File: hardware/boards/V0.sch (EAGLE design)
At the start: 61 parts, among them IC2 TPS6300, J1 SJ-43515TS-SMT, J2 HIROSE_DM3BT-DSF-PEJSHIROSE_D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, J3 MOLEX_105450-0101MOLEX_105450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, Q1 MC-306, Q2 ON_SEMI_MMBT5551LT1GON_SEMI_M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, U1 VS1053-L, X1 PG203J, X3 FH12-45S-0.5SH

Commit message: checkpoint: USB
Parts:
- added C21: 0.1uF, rcl:C-USC0805K
- added C22, C24: 4.7uF, rcl:CPOL-USC/6032-28R
- added C23, C25: 0.1uF, rcl:CPOL-USC/6032-28R
- added CENTER_SW, DOWN_SW, LEFT_SW, RIGHT_SW, UP_SW: E-SWITCH_TL3315NF160QE-SWITCH_TL3315NF160Q_0_0, E-Switch-TL3315NF160Q:E-SWITCH_TL3315NF160QE-SWITCH_TL3315NF160Q_0_0
- added D10, D8, D9: ON_SEMICONDUCTOR_ESD5Z5.0T1GON_SEMICONDUCTOR_ESD5Z5.0T1G_0_0, ESD-Diode_On-Semi-ESD5Z5.0T1G:ON_SEMICONDUCTOR_ESD5Z5.0T1GON_SEMICONDUCTOR_ESD5Z5.0T1G_0_0
- added D3, D4, D5, D6, D7: (no value), adafruit:DIODESOD-523
- added R19, R25, R33: 5k, rcl:R-US_R0805
- added R20: 15k, rcl:R-US_R0805
- added R21: 35k, rcl:R-US_R0805
- added R22: 75k, rcl:R-US_R0805
- added R23: 155k, rcl:R-US_R0805
- added R24: 50k, rcl:R-US_R0805
- added R26, R32: 10k, rcl:R-US_R0805
- added R27, R28: 5.1k, rcl:R-US_R0805
- added R29: 22.1k, rcl:R-US_R0805
- added R30: 47.5k, rcl:R-US_R0805
- added R31: 1k, rcl:R-US_R0805
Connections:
- new net BUTTON_ADC: R19.1, R20.1, R21.1, R22.1, R23.1, R25.2
- new net BUTTON_DIN: C21.2, R24.2
- new net CP_VDD: C24.+, C25.+, JL.VDD, R31.2
- new net N$16: D3.A, LEFT_SW.4, R19.2
- new net N$24: D4.A, R20.2, UP_SW.4
- new net N$28: D5.A, R21.2, RIGHT_SW.4
- new net N$29: D6.A, DOWN_SW.4, R22.2
- new net N$32: D3.C, D4.C, D5.C, D6.C, D7.C, R24.1, R26.2
- new net N$49: CENTER_SW.4, D7.A, R23.2
- new net N$50: J3.CC1, R27.1
- new net N$51: J3.CC2, R28.1
- new net N$52: JL.VBUS, R29.1, R30.2
- new net N$53: JL.RSTB, R31.1
- new net USB_D+: D9.K, J3.1_D+, J3.2_D+, JL.D+
- new net USB_D-: D8.K, J3.1_D-, J3.2_D-, JL.D-
- new net VBAT_ADC_IN: R32.2, R33.1
- new net VBUS: D10.K, J3.1_VBUS, J3.2_VBUS, J3.3_VBUS, J3.4_VBUS, R29.2
- net GND: now also C22.-, C23.-, C24.-, C25.-, D10.A, D8.A, D9.A, J3.1_GND, J3.2_GND, J3.3_GND, J3.4_GND, J3.MNT_1, J3.MNT_2, J3.MNT_3, J3.MNT_4, R25.1, R26.1, R27.2, R28.2, R30.1, R32.1
- net V3P3: now also C21.1, CENTER_SW.2, D1.COMMON_ANODE, DOWN_SW.2, LEFT_SW.2, RIGHT_SW.2, UP_SW.2
- net VBAT: now also C22.+, C23.+, JL.VREGIN, R33.2
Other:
- note added: "CC1"
- note added: "CC2"

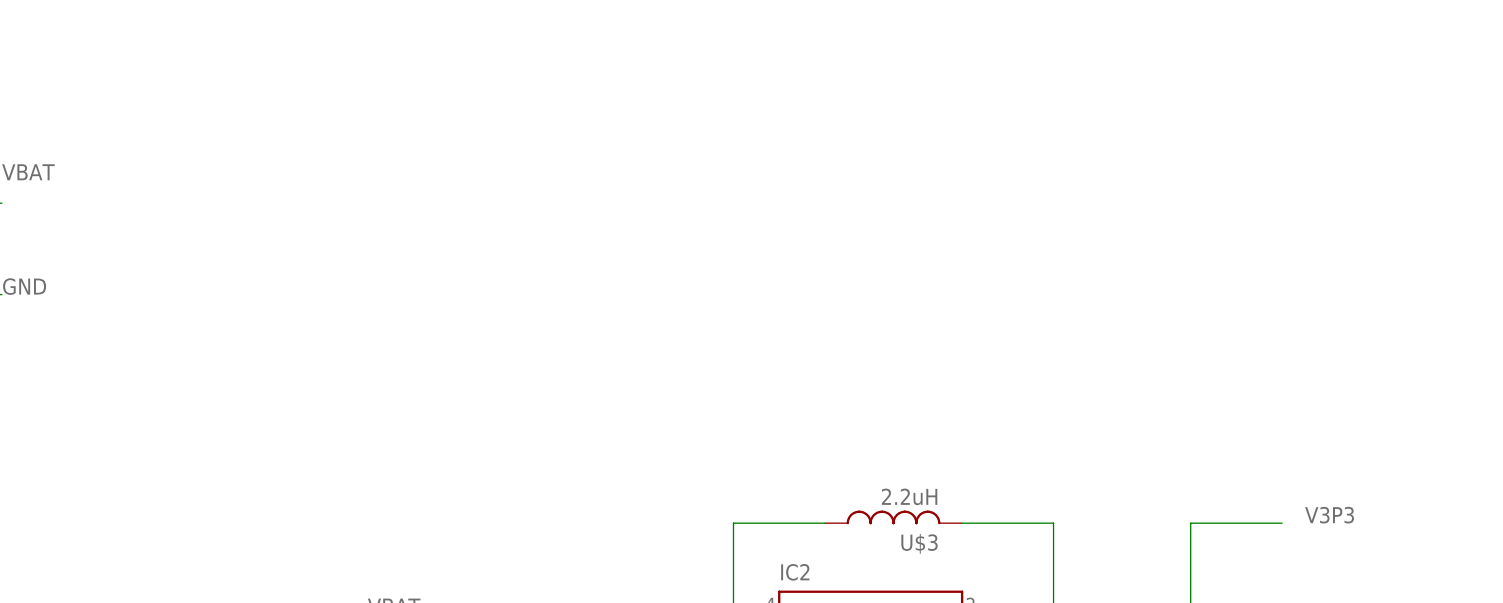
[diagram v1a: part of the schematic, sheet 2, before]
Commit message: checkpoint: LED, battery voltage circuit, charge IC, half of the CP2102N
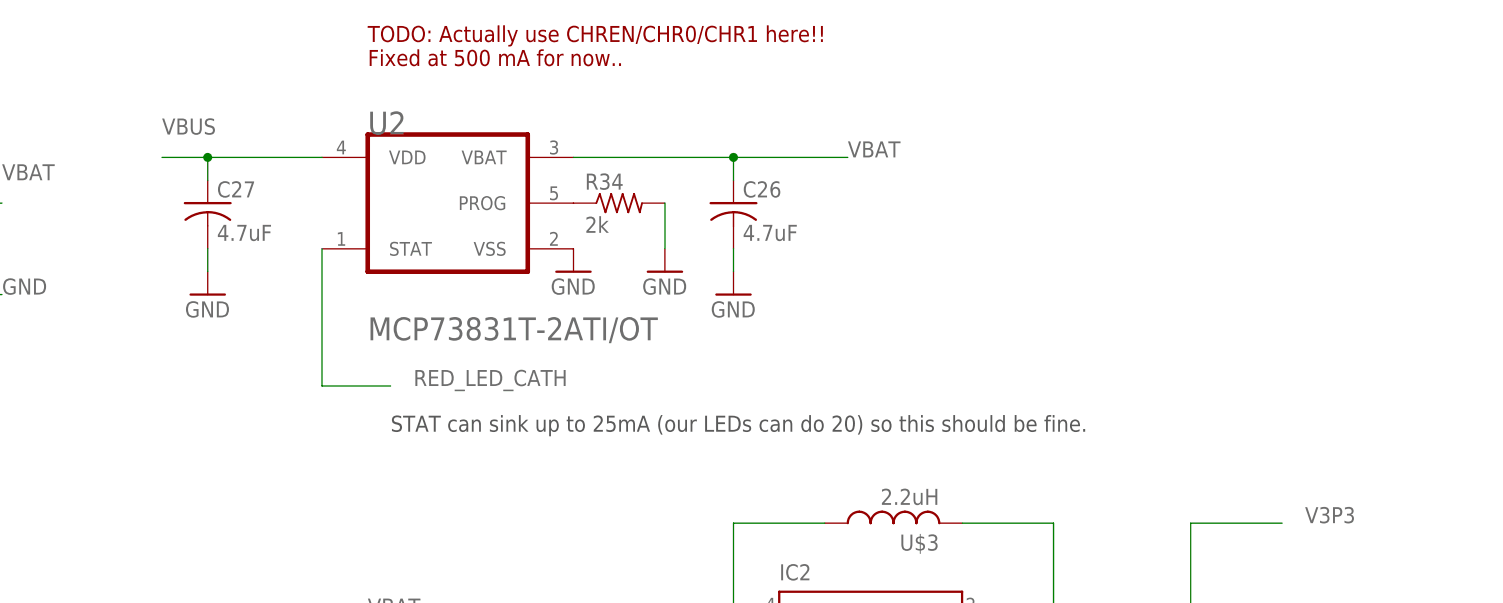
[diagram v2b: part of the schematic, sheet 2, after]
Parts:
- added C26, C27: 4.7uF, rcl:C-USC0805
- added R34: 2k, rcl:R-US_R0805
- added R35: 100, rcl:R-US_R0805
- added R36: (no value), rcl:R-US_R0805
- added U2: MICROCHIP_MCP73831T-2ATI-OTMICROCHIP_MCP73831T-2ATI-OT_0_1, Microchip-MCP73831T-2ATI:MICROCHIP_MCP73831T-2ATI-OTMICROCHIP_MCP73831T-2ATI-OT_0_1
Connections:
- new net BLUE_LED_CATH: D1.BLUE_CATHODE
- new net GREEN_LED_CATH: R36.2
- new net N$54: R34.1, U2.PROG
- new net N$55: D1.RED_CATHODE, R35.1
- new net N$56: D1.GREEN_CATHODE, R36.1
- new net RED_LED_CATH: R35.2, U2.STAT
- net GND: now also C26.2, C27.2, R34.2, U2.VSS
- net VBAT: now also C26.1, U2.VBAT
- net VBUS: now also C27.1, U2.VDD
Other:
- note added: "Blue has a voltage drop of ~3.7V which is greater than our regulated voltage so we won't bother with a current limiting resistor."
- note added: "Green LED (AlInGaP Green on the C113) has a drop of about 2.3 volts also on about 20mA. 1.0 volts for 20mA = V / I = R = 1 / 20mA = 50 ohms"
- note added: "Red LED has a 1.9V drop and 20mA, so: 1.4V for 20mA = V / I = R = 1.4V / 20mA = 70 ohms since we don't want to blind people let's call it an even 100"
- note added: "STAT can sink up to 25mA (our LEDs can do 20) so this should be fine."
- note added: "TODO: Actually use CHREN/CHR0/CHR1 here!! Fixed at 500 mA for now.."
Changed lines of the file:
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@@
 <part name="R32" library="rcl" library_urn="urn:adsk.eagle:library:334" deviceset="R-US_" device="R0805" package3d_urn="urn:adsk.eagle:package:23553/2" value="10k"/>
 <part name="R33" library="rcl" library_urn="urn:adsk.eagle:library:334" deviceset="R-US_" device="R0805" package3d_urn="urn:adsk.eagle:package:23553/2" value="5k"/>
+<part name="U2" library="Microchip-MCP73831T-2ATI" deviceset="MICROCHIP_MCP73831T-2ATI-OT" device="MICROCHIP_MCP73831T-2ATI-OT_0_1"/>
+<part name="C26" library="rcl" library_urn="urn:adsk.eagle:library:334" deviceset="C-US" device="C0805" package3d_urn="urn:adsk.eagle:package:23617/2" value="4.7uF"/>
+<part name="GND27" library="supply1" library_urn="urn:adsk.eagle:library:371" deviceset="GND" device=""/>
+<part name="GND28" library="supply1" library_urn="urn:adsk.eagle:library:371" deviceset="GND" device=""/>
+<part name="GND29" library="supply1" library_urn="urn:adsk.eagle:library:371" deviceset="GND" device=""/>
+<part name="R34" library="rcl" library_urn="urn:adsk.eagle:library:334" deviceset="R-US_" device="R0805" package3d_urn="urn:adsk.eagle:package:23553/2" value="2k"/>
+<part name="C27" library="rcl" library_urn="urn:adsk.eagle:library:334" deviceset="C-US" device="C0805" package3d_urn="urn:adsk.eagle:package:23617/2" value="4.7uF"/>
+<part name="GND30" library="supply1" library_urn="urn:adsk.eagle:library:371" deviceset="GND" device=""/>
+<part name="R35" library="rcl" library_urn="urn:adsk.eagle:library:334" deviceset="R-US_" device="R0805" package3d_urn="urn:adsk.eagle:package:23553/2" value="100"/>
+<part name="R36" library="rcl" library_urn="urn:adsk.eagle:library:334" deviceset="R-US_" device="R0805" package3d_urn="urn:adsk.eagle:package:23553/2"/>
 </parts>
 <sheets>
@@
 <plain>
 <text x="30.48" y="-7.62" size="1.778" layer="95">TPS6224</text>
+<text x="-83.82" y="71.12" size="1.778" layer="94">TODO: Actually use CHREN/CHR0/CHR1 here!!
+Fixed at 500 mA for now..</text>
+<text x="-81.28" y="30.48" size="1.778" layer="97">STAT can sink up to 25mA (our LEDs can do 20) so this should be fine.</text>
 </plain>
 <instances>
@@
 <instance part="BATT_CON" gate="G$0" x="-149.86" y="66.04" smashed="yes">
 <attribute name="NAME" x="-147.32" y="63.5" size="2.54" layer="95" align="top-left"/>
+</instance>
+<instance part="U2" gate="G$0" x="-83.82" y="68.58" smashed="yes">
+<attribute name="NAME" x="-83.82" y="66.04" size="2.54" layer="95" align="top-left"/>
+</instance>
+<instance part="C26" gate="G$1" x="-43.18" y="55.88" smashed="yes">
+<attribute name="NAME" x="-42.164" y="56.515" size="1.778" layer="95"/>
+<attribute name="VALUE" x="-42.164" y="51.689" size="1.778" layer="96"/>
+</instance>
+<instance part="GND27" gate="1" x="-43.18" y="45.72" smashed="yes">
+<attribute name="VALUE" x="-45.72" y="43.18" size="1.778" layer="96"/>
+</instance>
+<instance part="GND28" gate="1" x="-60.96" y="48.26" smashed="yes">
+<attribute name="VALUE" x="-63.5" y="45.72" size="1.778" layer="96"/>
+</instance>
+<instance part="GND29" gate="1" x="-50.8" y="48.26" smashed="yes">
+<attribute name="VALUE" x="-53.34" y="45.72" size="1.778" layer="96"/>
+</instance>
+<instance part="R34" gate="G$1" x="-55.88" y="55.88" smashed="yes">
+<attribute name="NAME" x="-59.69" y="57.3786" size="1.778" layer="95"/>
+<attribute name="VALUE" x="-59.69" y="52.578" size="1.778" layer="96"/>
+</instance>
+<instance part="C27" gate="G$1" x="-101.6" y="55.88" smashed="yes">
+<attribute name="NAME" x="-100.584" y="56.515" size="1.778" layer="95"/>
+<attribute name="VALUE" x="-100.584" y="51.689" size="1.778" layer="96"/>
+</instance>
+<instance part="GND30" gate="1" x="-101.6" y="45.72" smashed="yes">
+<attribute name="VALUE" x="-104.14" y="43.18" size="1.778" layer="96"/>
 </instance>
 </instances>
@@
 <wire x1="-129.54" y1="55.88" x2="-124.46" y2="55.88" width="0.1524" layer="91"/>
 <label x="-124.46" y="58.42" size="1.778" layer="95"/>
+</segment>
+<segment>
+<pinref part="U2" gate="G$0" pin="VBAT"/>
+<wire x1="-60.96" y1="60.96" x2="-43.18" y2="60.96" width="0.1524" layer="91"/>
+<pinref part="C26" gate="G$1" pin="1"/>
+<wire x1="-43.18" y1="60.96" x2="-43.18" y2="58.42" width="0.1524" layer="91"/>
+<wire x1="-43.18" y1="60.96" x2="-30.48" y2="60.96" width="0.1524" layer="91"/>
+<junction x="-43.18" y="60.96"/>
+<label x="-30.48" y="60.96" size="1.778" layer="95"/>
 </segment>
 </net>
@@
 <junction x="-127" y="40.64"/>
 </segment>
+<segment>
+<pinref part="GND27" gate="1" pin="GND"/>
+<pinref part="C26" gate="G$1" pin="2"/>
+<wire x1="-43.18" y1="48.26" x2="-43.18" y2="50.8" width="0.1524" layer="91"/>
+</segment>
+<segment>
+<pinref part="U2" gate="G$0" pin="VSS"/>
+<pinref part="GND28" gate="1" pin="GND"/>
+</segment>
+<segment>
+<pinref part="R34" gate="G$1" pin="2"/>
+<pinref part="GND29" gate="1" pin="GND"/>
+<wire x1="-50.8" y1="55.88" x2="-50.8" y2="50.8" width="0.1524" layer="91"/>
+</segment>
+<segment>
+<pinref part="C27" gate="G$1" pin="2"/>
+<pinref part="GND30" gate="1" pin="GND"/>
+<wire x1="-101.6" y1="48.26" x2="-101.6" y2="50.8" width="0.1524" layer="91"/>
+</segment>
 </net>
 <net name="V1P8" class="0">
@@
 <pinref part="TPS6224" gate="G$1" pin="SW"/>
 <pinref part="U$5" gate="G$1" pin="1"/>
+</segment>
+</net>
+<net name="N$54" class="0">
+<segment>
+<pinref part="U2" gate="G$0" pin="PROG"/>
+<pinref part="R34" gate="G$1" pin="1"/>
+</segment>
+</net>
+<net name="VBUS" class="0">
+<segment>
+<pinref part="C27" gate="G$1" pin="1"/>
+<wire x1="-101.6" y1="58.42" x2="-101.6" y2="60.96" width="0.1524" layer="91"/>
+<pinref part="U2" gate="G$0" pin="VDD"/>
+<wire x1="-101.6" y1="60.96" x2="-88.9" y2="60.96" width="0.1524" layer="91"/>
+<junction x="-101.6" y="60.96"/>
+<wire x1="-101.6" y1="60.96" x2="-106.68" y2="60.96" width="0.1524" layer="91"/>
+<label x="-106.68" y="63.5" size="1.778" layer="95"/>
+</segment>
+</net>
+<net name="RED_LED_CATH" class="0">
+<segment>
+<pinref part="U2" gate="G$0" pin="STAT"/>
+<wire x1="-88.9" y1="50.8" x2="-88.9" y2="35.56" width="0.1524" layer="91"/>
+<wire x1="-88.9" y1="35.56" x2="-81.28" y2="35.56" width="0.1524" layer="91"/>
+<label x="-78.74" y="35.56" size="1.778" layer="95"/>
 </segment>
 </net>
@@
 (Line In Controls, LED, Battery Voltage)</description>
 <plain>
+<text x="-35.56" y="22.86" size="1.778" layer="97">Red LED has a 1.9V drop and 20mA, so:
+1.4V for 20mA = V / I = R = 1.4V / 20mA = 70 ohms
+since we don't want to blind people let's call it an even 100</text>
+<text x="-38.1" y="-30.48" size="1.778" layer="97">Green LED (AlInGaP Green on the C113) has a drop of about 2.3 volts also on about 20mA.
+1.0 volts for 20mA = V / I = R = 1 / 20mA = 50 ohms</text>
+<text x="-38.1" y="-38.1" size="1.778" layer="97">Blue has a voltage drop of ~3.7V which is greater than our regulated voltage so we won't bother with a current limiting resistor.</text>
 </plain>
 <instances>
@@
 <attribute name="NAME" x="41.6814" y="6.35" size="1.778" layer="95" rot="R90"/>
 <attribute name="VALUE" x="46.482" y="6.35" size="1.778" layer="96" rot="R90"/>
+</instance>
+<instance part="R35" gate="G$1" x="-2.54" y="0" smashed="yes">
+<attribute name="NAME" x="-6.35" y="1.4986" size="1.778" layer="95"/>
+<attribute name="VALUE" x="-6.35" y="-3.302" size="1.778" layer="96"/>
+</instance>
+<instance part="R36" gate="G$1" x="-2.54" y="-10.16" smashed="yes">
+<attribute name="NAME" x="-6.35" y="-8.6614" size="1.778" layer="95"/>
+<attribute name="VALUE" x="-6.35" y="-13.462" size="1.778" layer="96"/>
 </instance>
 </instances>
@@
 </segment>
 </net>
+<net name="N$55" class="0">
+<segment>
+<pinref part="D1" gate="G$0" pin="RED_CATHODE"/>
+<pinref part="R35" gate="G$1" pin="1"/>
+<wire x1="-10.16" y1="0" x2="-7.62" y2="0" width="0.1524" layer="91"/>
+</segment>
+</net>
+<net name="RED_LED_CATH" class="0">
+<segment>
+<pinref part="R35" gate="G$1" pin="2"/>
+<wire x1="2.54" y1="0" x2="7.62" y2="0" width="0.1524" layer="91"/>
+<label x="7.62" y="0" size="1.778" layer="95"/>
+</segment>
+</net>
+<net name="N$56" class="0">
+<segment>
+<pinref part="D1" gate="G$0" pin="GREEN_CATHODE"/>
+<pinref part="R36" gate="G$1" pin="1"/>
+<wire x1="-10.16" y1="-10.16" x2="-7.62" y2="-10.16" width="0.1524" layer="91"/>
+</segment>
+</net>
+<net name="GREEN_LED_CATH" class="0">
+<segment>
+<pinref part="R36" gate="G$1" pin="2"/>
+<wire x1="2.54" y1="-10.16" x2="7.62" y2="-10.16" width="0.1524" layer="91"/>
+<label x="7.62" y="-10.16" size="1.778" layer="95"/>
+</segment>
+</net>
+<net name="BLUE_LED_CATH" class="0">
+<segment>
+<pinref part="D1" gate="G$0" pin="BLUE_CATHODE"/>
+<wire x1="-10.16" y1="10.16" x2="7.62" y2="10.16" width="0.1524" layer="91"/>
+<label x="7.62" y="10.16" size="1.778" layer="95"/>
+</segment>
+</net>

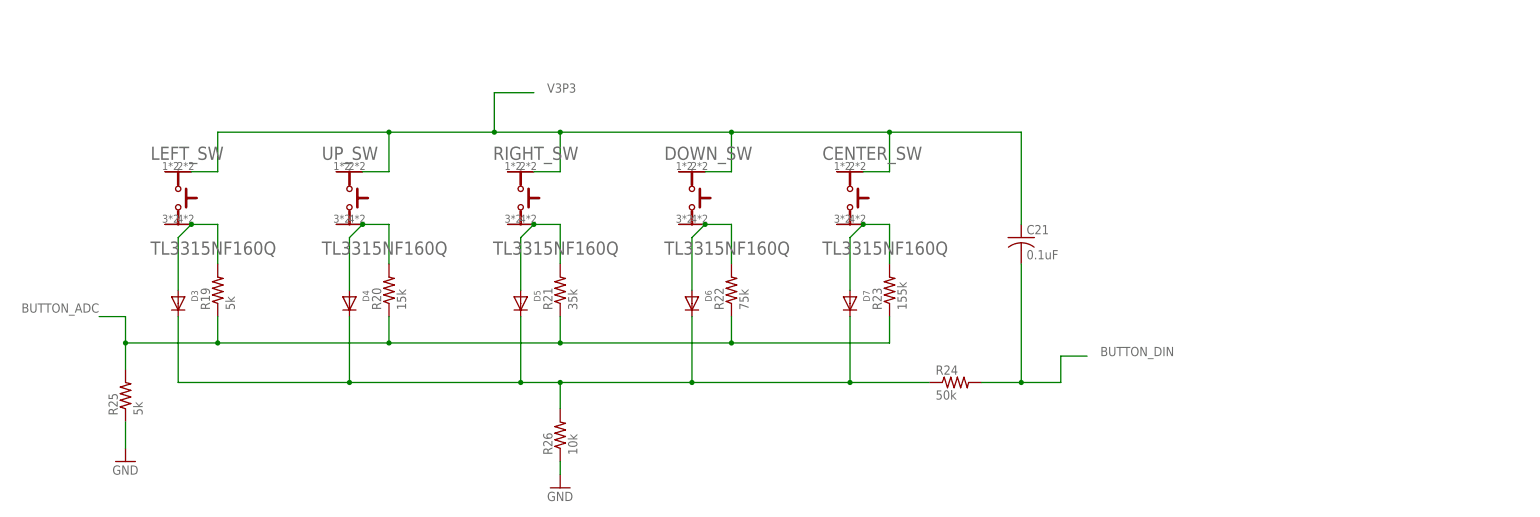
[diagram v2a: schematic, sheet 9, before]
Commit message: checkpoint: power on and off circuit
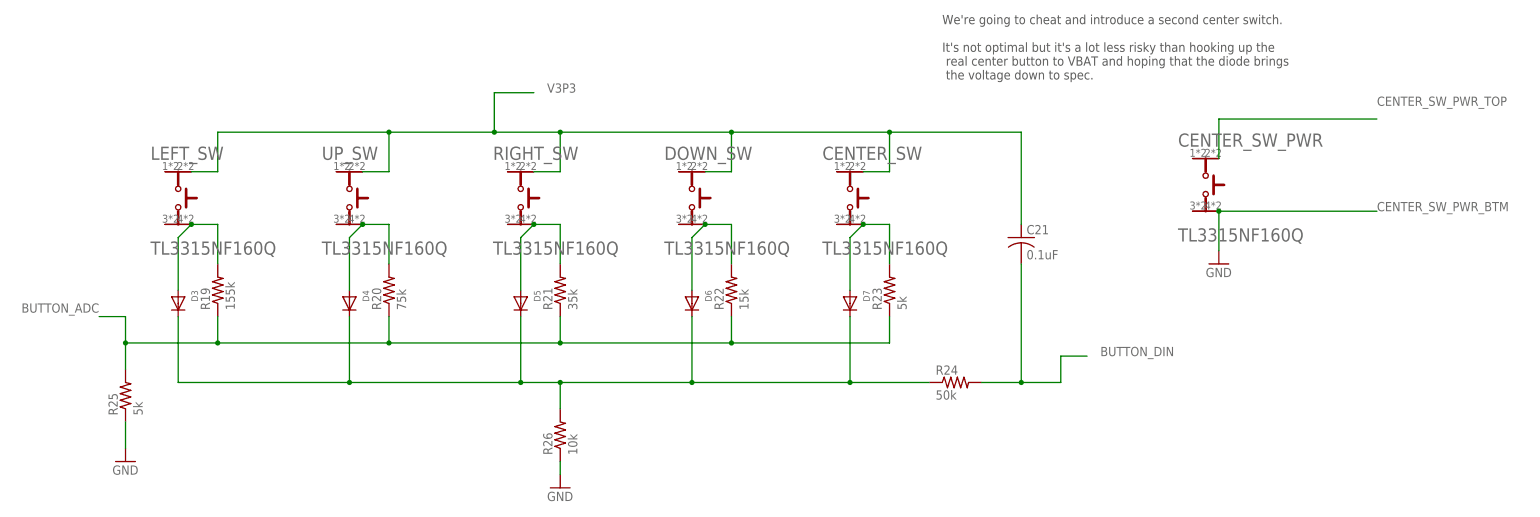
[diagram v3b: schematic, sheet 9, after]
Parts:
- removed SW1: (no value), adafruit:SWITCH_PUSHBUTTONSOFTTOUCHSMD_SJ
- added CENTER_SW_PWR: E-SWITCH_TL3315NF160QE-SWITCH_TL3315NF160Q_0_0, E-Switch-TL3315NF160Q:E-SWITCH_TL3315NF160QE-SWITCH_TL3315NF160Q_0_0
- C6, C7: device adafruit:C-US025-024X044 -> rcl:C-USC1206
- R10, R9: device adafruit:R-US_0204/2V -> rcl:R-US_R0805
- R11: device adafruit:R-US_R3216 -> rcl:R-US_R0805
- R19: value 5k -> 155k
- R20: value 15k -> 75k
- R22: value 75k -> 15k
- R23: value 155k -> 5k
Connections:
- net N$49 renamed CENTER_SW
- removed net N$11: R10.2, R9.2
- removed net N$18: U$2.1Y, U$2.2B
- removed net N$20: U$2.VCC
- removed net N$21: U$2.GND
- removed net N$23: R11.1, SW1.P$2
- new net CENTER_SW_PWR_BTM: CENTER_SW_PWR.4
- new net CENTER_SW_PWR_TOP: CENTER_SW_PWR.2, R11.1
- new net SYS_ENABLE: IC2G$1.EN, U$2.1Y, U$2.2B
- net GND: now also U$2.GND; no longer SW1.P$1
- net N$3: no longer IC2G$1.EN
- net VBAT: now also R10.2, R9.2, U$2.VCC
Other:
- note added: "(pos logic enable)"
- note added: "This chip is 5.5V tolerant so we're okay running it off of VBAT. EN on the regulator is 7V tolerant so that's fine too."
- note added: "We're going to cheat and introduce a second center switch. It's not optimal but it's a lot less risky than hooking up the real center button to VBAT and hoping that the diode brings the voltage down to spec."
- note removed: "GND"
- note removed: "V+"
- note removed: "V3P3"
- note removed: "Vout"
